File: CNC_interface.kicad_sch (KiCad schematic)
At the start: 25 parts, among them J1 Conn_01x04_Male, J10 Conn_01x08, J11 Conn_01x08, J12 Conn_01x08, J13 Conn_01x08, J14 Conn_01x03_Male, J15 Conn_01x03_Male, J16 Conn_01x03_Male, J17 Conn_01x08, J18 Conn_01x10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

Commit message: place components on pcb
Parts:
- J4, J5, J6: footprint CNC_interface:TerminalBlock_Phoenix_MKDSP-1,5-2-5.08_1x02_P5.08mm -> CNC_interface:RS_pro_screw_terminal_P5.08_x2
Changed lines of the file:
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@@
       (effects (font (size 1.27 1.27)) (justify left))
     )
-    (property "Footprint" "CNC_interface:TerminalBlock_Phoenix_MKDSP-1,5-2-5.08_1x02_P5.08mm" (id 2) (at 46.99 31.75 0)
+    (property "Footprint" "CNC_interface:RS_pro_screw_terminal_P5.08_x2" (id 2) (at 46.99 31.75 0)
       (effects (font (size 1.27 1.27)) hide)
     )
@@
       (effects (font (size 1.27 1.27)) (justify left))
     )
-    (property "Footprint" "CNC_interface:TerminalBlock_Phoenix_MKDSP-1,5-2-5.08_1x02_P5.08mm" (id 2) (at 46.99 41.91 0)
+    (property "Footprint" "CNC_interface:RS_pro_screw_terminal_P5.08_x2" (id 2) (at 46.99 41.91 0)
       (effects (font (size 1.27 1.27)) hide)
     )
@@
       (effects (font (size 1.27 1.27)) (justify left))
     )
-    (property "Footprint" "CNC_interface:TerminalBlock_Phoenix_MKDSP-1,5-2-5.08_1x02_P5.08mm" (id 2) (at 50.8 114.3 0)
+    (property "Footprint" "CNC_interface:RS_pro_screw_terminal_P5.08_x2" (id 2) (at 50.8 114.3 0)
       (effects (font (size 1.27 1.27)) hide)
     )
@@
     )
     (path "/f6130a08-de36-4d6d-b8cc-dfef4890d083"
-      (reference "J4") (unit 1) (value "Screw_Terminal_01x02") (footprint "CNC_interface:TerminalBlock_Phoenix_MKDSP-1,5-2-5.08_1x02_P5.08mm")
+      (reference "J4") (unit 1) (value "Screw_Terminal_01x02") (footprint "CNC_interface:RS_pro_screw_terminal_P5.08_x2")
     )
     (path "/00000000-0000-0000-0000-00006208728f"
-      (reference "J5") (unit 1) (value "Screw_Terminal_01x02") (footprint "CNC_interface:TerminalBlock_Phoenix_MKDSP-1,5-2-5.08_1x02_P5.08mm")
+      (reference "J5") (unit 1) (value "Screw_Terminal_01x02") (footprint "CNC_interface:RS_pro_screw_terminal_P5.08_x2")
     )
     (path "/00000000-0000-0000-0000-000062087887"
-      (reference "J6") (unit 1) (value "Screw_Terminal_01x02") (footprint "CNC_interface:TerminalBlock_Phoenix_MKDSP-1,5-2-5.08_1x02_P5.08mm")
+      (reference "J6") (unit 1) (value "Screw_Terminal_01x02") (footprint "CNC_interface:RS_pro_screw_terminal_P5.08_x2")
     )
     (path "/00000000-0000-0000-0000-00006208cce0"
@@
     )
     (path "/8b7d305c-caee-4338-94fc-4790d784af7f/9264dc6e-5915-4d3e-9e3c-68b480f21536"
-      (reference "L1") (unit 1) (value "150µF") (footprint "Inductor_SMD:L_TDK_SLF10145")
+      (reference "L1") (unit 1) (value "150µF") (footprint "CNC_interface:L_Radial_24.4mm_P23.50mm_Murata_1400series")
     )
     (path "/8b7d305c-caee-4338-94fc-4790d784af7f/6ef44ea8-e69c-45bc-be4d-863f0548e8f5"
-      (reference "L4") (unit 1) (value "220µH") (footprint "Inductor_SMD:L_TDK_SLF10145")
+      (reference "L2") (unit 1) (value "220µH") (footprint "CNC_interface:L_Radial_24.4mm_P23.50mm_Murata_1400series")
     )
     (path "/00000000-0000-0000-0000-000062070cd9"

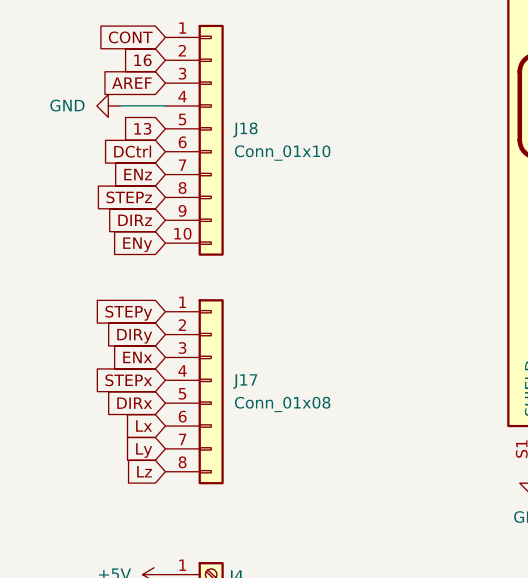
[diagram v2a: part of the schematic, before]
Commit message: route pcb + GND floorplan
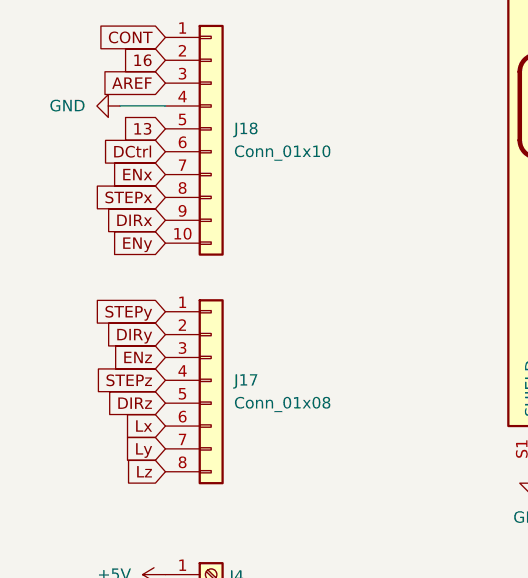
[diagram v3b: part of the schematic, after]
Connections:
- net DIRx: now also J18.9 (Pin_9); no longer J17.5 (Pin_5)
- net DIRz: now also J17.5 (Pin_5); no longer J18.9 (Pin_9)
- net ENx: now also J18.7 (Pin_7); no longer J17.3 (Pin_3)
- net ENz: now also J17.3 (Pin_3); no longer J18.7 (Pin_7)
- net STEPx: now also J18.8 (Pin_8); no longer J17.4 (Pin_4)
- net STEPz: now also J17.4 (Pin_4); no longer J18.8 (Pin_8)
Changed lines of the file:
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@@
     )
   )
-  (global_label "DIRx" (shape input) (at 45.72 95.25 180) (fields_autoplaced)
+  (global_label "DIRz" (shape input) (at 45.72 95.25 180) (fields_autoplaced)
     (effects (font (size 1.27 1.27)) (justify right))
     (property "Intersheet References" "${INTERSHEET_REFS}" (id 0) (at 39.2229 95.1706 0)
@@
     )
   )
-  (global_label "DIRz" (shape input) (at 45.72 74.93 180) (fields_autoplaced)
+  (global_label "DIRx" (shape input) (at 45.72 74.93 180) (fields_autoplaced)
     (effects (font (size 1.27 1.27)) (justify right))
     (property "Intersheet References" "${INTERSHEET_REFS}" (id 0) (at 39.2229 74.8506 0)
@@
     )
   )
-  (global_label "ENx" (shape input) (at 45.72 90.17 180) (fields_autoplaced)
+  (global_label "ENz" (shape input) (at 45.72 90.17 180) (fields_autoplaced)
     (effects (font (size 1.27 1.27)) (justify right))
     (property "Intersheet References" "${INTERSHEET_REFS}" (id 0) (at 39.8882 90.0906 0)
@@
     )
   )
-  (global_label "STEPx" (shape input) (at 45.72 92.71 180) (fields_autoplaced)
+  (global_label "STEPz" (shape input) (at 45.72 92.71 180) (fields_autoplaced)
     (effects (font (size 1.27 1.27)) (justify right))
     (property "Intersheet References" "${INTERSHEET_REFS}" (id 0) (at 37.7715 92.6306 0)
@@
     )
   )
-  (global_label "ENz" (shape input) (at 45.72 69.85 180) (fields_autoplaced)
+  (global_label "ENx" (shape input) (at 45.72 69.85 180) (fields_autoplaced)
     (effects (font (size 1.27 1.27)) (justify right))
     (property "Intersheet References" "${INTERSHEET_REFS}" (id 0) (at 39.8882 69.7706 0)
@@
     )
   )
-  (global_label "STEPz" (shape input) (at 45.72 72.39 180) (fields_autoplaced)
+  (global_label "STEPx" (shape input) (at 45.72 72.39 180) (fields_autoplaced)
     (effects (font (size 1.27 1.27)) (justify right))
     (property "Intersheet References" "${INTERSHEET_REFS}" (id 0) (at 37.7715 72.3106 0)

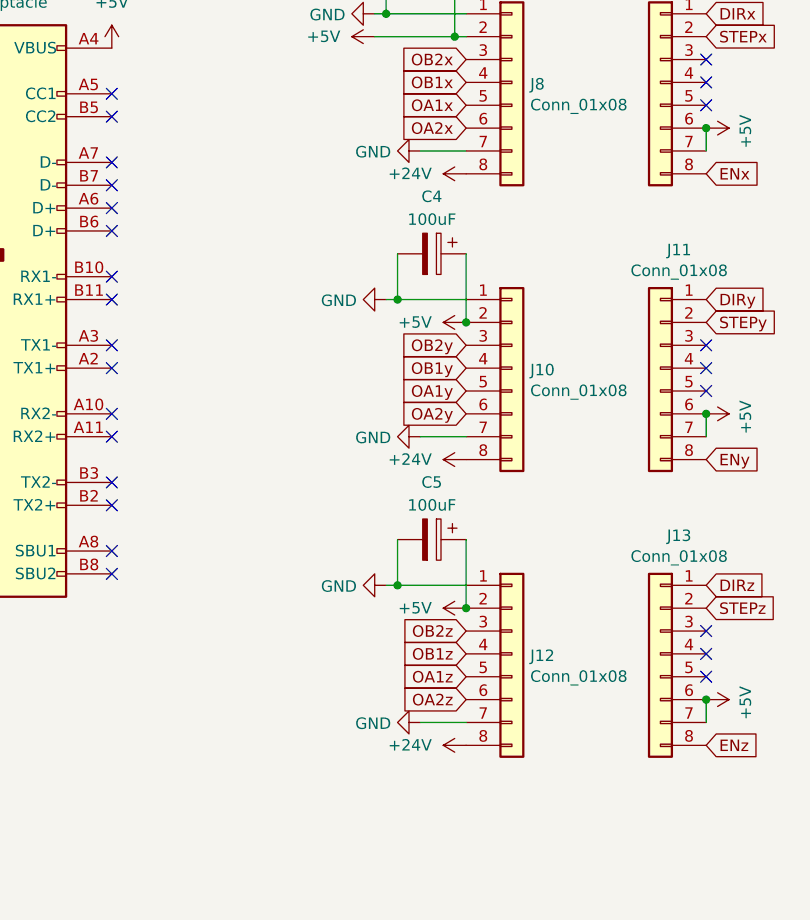
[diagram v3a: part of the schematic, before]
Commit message: connect step motors to 12V
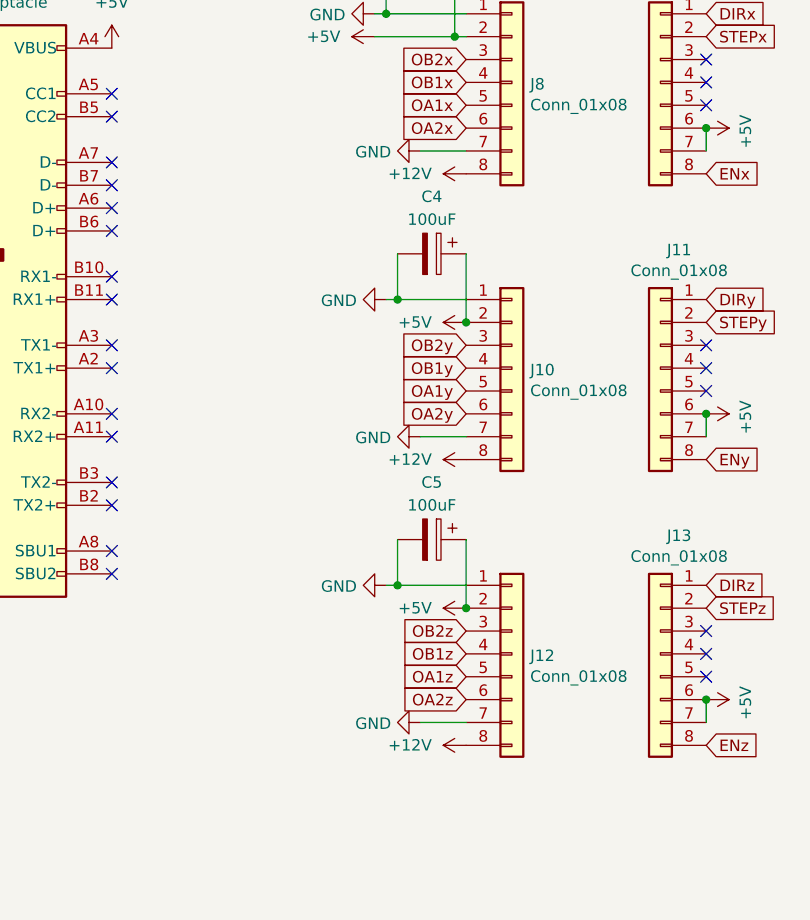
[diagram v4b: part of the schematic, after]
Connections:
- net +12V: now also J10.8 (Pin_8), J12.8 (Pin_8), J8.8 (Pin_8)
- net +24V: no longer J10.8 (Pin_8), J12.8 (Pin_8), J8.8 (Pin_8)
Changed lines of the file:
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@@
     (pin "1")
   )
-  (symbol (lib_id "power:+24V") (at 148.59 82.55 90) (unit 1)
-    (in_bom yes) (on_board yes) (fields_autoplaced)
-    (property "Reference" "#PWR0132" (id 0) (at 152.4 82.55 0)
-      (effects (font (size 1.27 1.27)) hide)
-    )
-    (property "Value" "+24V" (id 1) (at 144.78 82.5499 90)
+  (symbol (lib_id "power:+12V") (at 148.59 82.55 90) (unit 1)
+    (in_bom yes) (on_board yes) (fields_autoplaced)
+    (property "Reference" "#PWR?" (id 0) (at 152.4 82.55 0)
+      (effects (font (size 1.27 1.27)) hide)
+    )
+    (property "Value" "+12V" (id 1) (at 144.78 82.5499 90)
       (effects (font (size 1.27 1.27)) (justify left))
     )
@@
     )
     (property "Datasheet" "" (id 3) (at 248.92 45.72 0)
-      (effects (font (size 1.27 1.27)) hide)
-    )
-    (pin "1")
-  )
-  (symbol (lib_id "power:+24V") (at 148.59 50.8 90) (unit 1)
-    (in_bom yes) (on_board yes) (fields_autoplaced)
-    (property "Reference" "#PWR0136" (id 0) (at 152.4 50.8 0)
-      (effects (font (size 1.27 1.27)) hide)
-    )
-    (property "Value" "+24V" (id 1) (at 144.78 50.7999 90)
-      (effects (font (size 1.27 1.27)) (justify left))
-    )
-    (property "Footprint" "" (id 2) (at 148.59 50.8 0)
-      (effects (font (size 1.27 1.27)) hide)
-    )
-    (property "Datasheet" "" (id 3) (at 148.59 50.8 0)
       (effects (font (size 1.27 1.27)) hide)
     )
@@
     (pin "1")
     (pin "2")
+  )
+  (symbol (lib_id "power:+12V") (at 148.59 50.8 90) (unit 1)
+    (in_bom yes) (on_board yes) (fields_autoplaced)
+    (property "Reference" "#PWR?" (id 0) (at 152.4 50.8 0)
+      (effects (font (size 1.27 1.27)) hide)
+    )
+    (property "Value" "+12V" (id 1) (at 144.78 50.7999 90)
+      (effects (font (size 1.27 1.27)) (justify left))
+    )
+    (property "Footprint" "" (id 2) (at 148.59 50.8 0)
+      (effects (font (size 1.27 1.27)) hide)
+    )
+    (property "Datasheet" "" (id 3) (at 148.59 50.8 0)
+      (effects (font (size 1.27 1.27)) hide)
+    )
+    (pin "1")
   )
   (symbol (lib_id "power:+5V") (at 148.59 67.31 90) (unit 1)
@@
     (pin "S1")
   )
-  (symbol (lib_id "power:+24V") (at 148.59 114.3 90) (unit 1)
-    (in_bom yes) (on_board yes) (fields_autoplaced)
-    (property "Reference" "#PWR0133" (id 0) (at 152.4 114.3 0)
-      (effects (font (size 1.27 1.27)) hide)
-    )
-    (property "Value" "+24V" (id 1) (at 144.78 114.2999 90)
+  (symbol (lib_id "power:+12V") (at 148.59 114.3 90) (unit 1)
+    (in_bom yes) (on_board yes) (fields_autoplaced)
+    (property "Reference" "#PWR?" (id 0) (at 152.4 114.3 0)
+      (effects (font (size 1.27 1.27)) hide)
+    )
+    (property "Value" "+12V" (id 1) (at 144.78 114.2999 90)
       (effects (font (size 1.27 1.27)) (justify left))
     )
@@
       (reference "#PWR0131") (unit 1) (value "+5V") (footprint "")
     )
-    (path "/31a71321-d9f9-464f-8dc0-ee065f4e0170"
-      (reference "#PWR0132") (unit 1) (value "+24V") (footprint "")
-    )
-    (path "/c0c1d321-59fb-4e73-a82d-6bc5798c0d11"
-      (reference "#PWR0133") (unit 1) (value "+24V") (footprint "")
-    )
     (path "/9cc3fedb-e7e4-4d83-84e3-7ed5b13ae7b5"
       (reference "#PWR0134") (unit 1) (value "+5V") (footprint "")
@@
       (reference "#PWR0135") (unit 1) (value "+5V") (footprint "")
     )
-    (path "/46f73811-9440-4704-af14-f571f794e5bd"
-      (reference "#PWR0136") (unit 1) (value "+24V") (footprint "")
-    )
     (path "/8b7d305c-caee-4338-94fc-4790d784af7f/2ac1aff8-0f18-45cf-83e1-f1a00fd60e7c"
       (reference "#PWR0137") (unit 1) (value "GND") (footprint "")
@@
       (reference "#PWR0147") (unit 1) (value "GND") (footprint "")
     )
+    (path "/306356ce-3d3d-4ee4-ab88-99af3cfd3700"
+      (reference "#PWR?") (unit 1) (value "+12V") (footprint "")
+    )
+    (path "/998f8fc2-f876-46d4-9582-c9487fcb3793"
+      (reference "#PWR?") (unit 1) (value "+12V") (footprint "")
+    )
+    (path "/ba652f01-eff8-486a-ad05-0601e550fdde"
+      (reference "#PWR?") (unit 1) (value "+12V") (footprint "")
+    )
     (path "/8b7d305c-caee-4338-94fc-4790d784af7f/0b74e936-0859-43e8-92e6-70d6886113e7"
-      (reference "C1") (unit 1) (value "100µF") (footprint "Capacitor_THT:CP_Radial_D12.5mm_P5.00mm")
+      (reference "C1") (unit 1) (value "100µF") (footprint "Capacitor_THT:CP_Radial_D6.3mm_P2.50mm")
     )
     (path "/8b7d305c-caee-4338-94fc-4790d784af7f/5d556b72-1d56-4ef9-801c-f56aab720ae4"
-      (reference "C2") (unit 1) (value "1000uF") (footprint "Capacitor_THT:CP_Radial_D8.0mm_P3.50mm")
+      (reference "C2") (unit 1) (value "1000uF") (footprint "Capacitor_THT:CP_Radial_D12.5mm_P5.00mm")
     )
     (path "/93b36e73-379e-4f68-bf56-ed3063cf9415"
@@
     )
     (path "/8b7d305c-caee-4338-94fc-4790d784af7f/38e766e3-8f0d-435f-85a7-b841375c9d0e"
-      (reference "C6") (unit 1) (value "100µF") (footprint "Capacitor_THT:CP_Radial_D12.5mm_P5.00mm")
+      (reference "C6") (unit 1) (value "100µF") (footprint "Capacitor_THT:CP_Radial_D6.3mm_P2.50mm")
     )
     (path "/8b7d305c-caee-4338-94fc-4790d784af7f/7f0debda-8e70-4f6a-ab19-a22319396f56"
-      (reference "C7") (unit 1) (value "1000µF") (footprint "Capacitor_THT:CP_Radial_D8.0mm_P3.50mm")
+      (reference "C7") (unit 1) (value "1000µF") (footprint "Capacitor_THT:CP_Radial_D12.5mm_P5.00mm")
     )
     (path "/00000000-0000-0000-0000-000062073139"
